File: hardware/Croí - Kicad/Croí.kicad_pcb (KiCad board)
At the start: 4 copper layers, 60 x 60 mm, 46 parts, among them J1 JTAG-10 PIN, J2 XT30PW-M, J3 ESQ-110-14-G-D, Q1 IPP060N06N, U1 W25Q128JVS, U2 ADXL375BCCZ, U3 STM32F072C8Tx, U4 BME680, U5 BMP390, U7 TLV70433DBVT, U8 TJA1051T-3, U9 LSM6DSO32TR

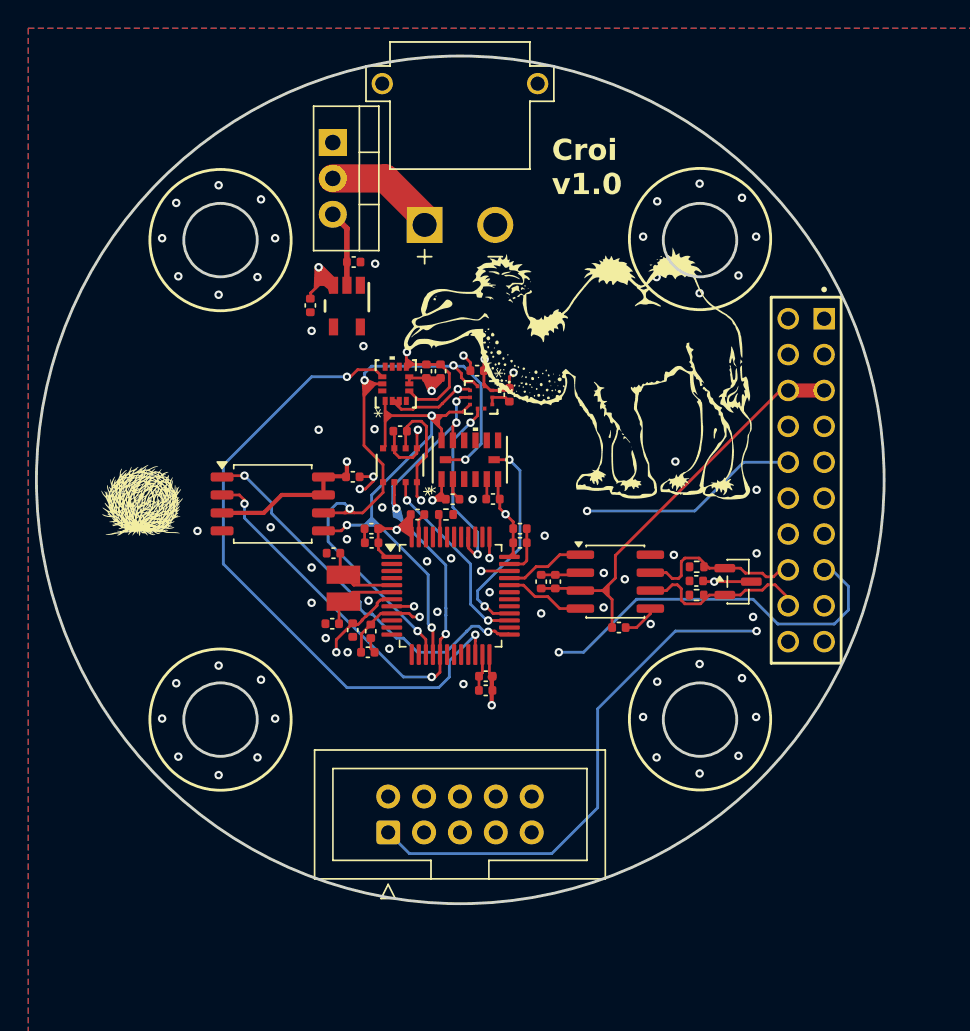
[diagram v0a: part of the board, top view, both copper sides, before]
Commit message: Started Applying Global Changes
1. Shape and screwholes
2. Mosfet
3. New Molex
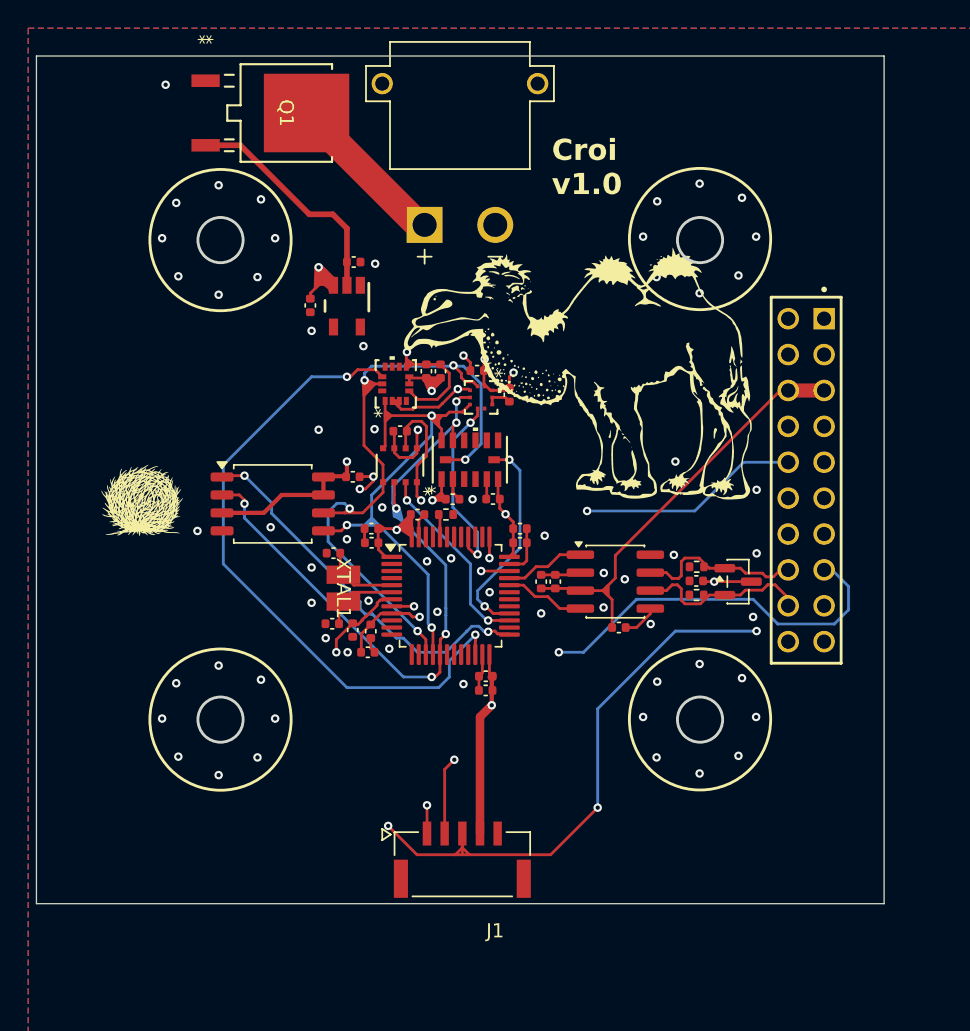
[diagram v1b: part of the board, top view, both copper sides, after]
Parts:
- J1: value JTAG-10 PIN -> 5023860570; footprint Connector_IDC:IDC-Header_2x05_P2.54mm_Vertical -> MOLEX:MOLEX_5023860570
- Q1: value IPP060N06N -> IPD90P04P4L04ATMA1; footprint Package_TO_SOT_THT:TO-220-3_Vertical -> footprints:PG-TO252-3-313_INF
- moved J1 5.63 mm to (73.0, 96.0), turned to 180 degrees
- moved Q1 3.90 mm to (60.5, 43.0)
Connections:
- J1 pad 1: NRST -> SWCLK2
- J1 pad 2: SWCLK2 -> SWDIO
- J1 pad 3: unconnected-(J1-Pin_3-Pad3) -> NRST
- J1 pad 4: SWDIO -> 3.3V
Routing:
- net VBAT: track 5.44 -> 16.5 mm
- net SWCLK2: track 48.4 -> 52.6 mm, vias 2 -> 3
- net NRST: track 62.8 -> 67.0 mm, vias 2 -> 4
- net Net-(Q1-D): track 7.66 -> 11.6 mm
- net SWDIO: track 55.3 -> 57.7 mm, vias 2 -> 3
- net 3.3V: track 154.3 -> 155.1 mm
- net (no net): vias 0 -> 1
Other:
- outline, holes or cut-outs redrawn

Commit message: Only missing one thing off the notion i believe, all 3d modlels should work
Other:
- board text added: "Croi v1.2"
- board text removed: "Croi v1.0"
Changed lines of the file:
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@@
 		(layer "Edge.Cuts")
 	)
-	(gr_text "Croi\nv1.0"
+	(gr_text "Croi\nv1.2"
 		(at 79.331 48.919 0)
 		(layer "F.SilkS")

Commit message: lots left to do, but good enough for render
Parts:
- removed U7: TLV70433DBVT, footprints:DBV0005A_M
- added 3v3: S2761-46R, footprints2:HARWIN_S2761-46R, F.Cu at (147.0, 79.8)
- added C+1: S2761-46R, footprints2:HARWIN_S2761-46R, F.Cu at (91.4, 73.6)
- added C-1: S2761-46R, footprints2:HARWIN_S2761-46R, F.Cu at (91.7, 78.8)
- added C14: 39pf, Capacitor_SMD:C_0402_1005Metric, F.Cu at (149.7, 63.5)
- added C16: 0.1uf, Capacitor_SMD:C_0402_1005Metric, F.Cu at (149.7, 65.5)
- added C29: 0.1uf, Capacitor_SMD:C_0402_1005Metric, F.Cu at (149.7, 71.4)
- added C30: 1uf, Capacitor_SMD:C_0402_1005Metric, F.Cu at (152.6, 63.5)
- added C31: 22uf, Capacitor_SMD:C_0402_1005Metric, F.Cu at (152.6, 65.5)
- added C32: 22uf, Capacitor_SMD:C_0402_1005Metric, F.Cu at (152.6, 67.5)
- added C33: 22uf, Capacitor_SMD:C_0402_1005Metric, F.Cu at (152.6, 69.4)
- added C34: 22uf, Capacitor_SMD:C_0402_1005Metric, F.Cu at (152.6, 71.4)
- added C35: 4.7uf, Capacitor_SMD:C_0402_1005Metric, F.Cu at (155.4, 63.5)
- added C36: 4.7uf, Capacitor_SMD:C_0402_1005Metric, F.Cu at (155.4, 65.5)
- added C37: 10uf, Capacitor_SMD:C_0402_1005Metric, F.Cu at (155.4, 67.5)
- added D1: BAT54C, Package_TO_SOT_SMD:SOT-23, F.Cu at (151.2, 80.7)
- added G***: LOGO, LOGO, F.Cu at (74.0, 88.5)
- added GND1: S2761-46R, footprints2:HARWIN_S2761-46R, F.Cu at (147.0, 82.3)
- added R10: 33.2kΩ, Resistor_SMD:R_0402_1005Metric, F.Cu at (146.8, 75.5)
- added R2: 10kΩ, Resistor_SMD:R_0402_1005Metric, F.Cu at (146.8, 63.5)
- added R3: 53.6kΩ, Resistor_SMD:R_0402_1005Metric, F.Cu at (146.8, 65.5)
- added R4: 0Ω, Resistor_SMD:R_0402_1005Metric, F.Cu at (146.8, 67.5)
- added R5: 0Ω, Resistor_SMD:R_0402_1005Metric, F.Cu at (146.8, 69.5)
- added R8: 499kΩ, Resistor_SMD:R_0402_1005Metric, F.Cu at (146.8, 71.5)
- added R9: 100kΩ, Resistor_SMD:R_0402_1005Metric, F.Cu at (146.8, 73.5)
- added U6: MPM3650CGQW-P, footprints2:QFN-24_MPM3650_MNP, F.Cu at (62.8, 63.3)
- added VR1: LT3045EDD_PBF, footprints2:SON50P300X300X80-11N, F.Cu at (63.9, 57.0)
- C21: value 100nF -> 22uf
- C23: value 1 uF -> 22uf
- moved C23 88.4 mm to (149.7, 69.4), turned to 0 degrees
- moved C21 85.5 mm to (149.7, 67.5)
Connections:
- C21 pad 1: VBAT -> GND
- C21 pad 2: GND -> /power/vin
- C23 pad 2: 3.3V -> /power/vin
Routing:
- net Net-(VR1-EN/UV): track 0.00 -> 19.3 mm
- net GND: track 46.4 -> 62.9 mm
- net 3.3V: track 155.1 -> 164.4 mm
- added copper zone on In3.Cu, net GND
- removed copper zone on In1.Cu, net GND
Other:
- copper layers 4 -> 6
- board text added: "SWCLK SWDIO NRST 3v3 GND"
- board text added: "croi-v1.0"
- board text removed: "Croi v1.2"

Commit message: running
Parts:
- removed the C35 at (155.4, 63.5)
- removed R10: 33.2kΩ, Resistor_SMD:R_0402_1005Metric
- removed the R4 at (146.8, 67.5)
- removed R5: 0Ω, Resistor_SMD:R_0402_1005Metric
- removed R8: 499kΩ, Resistor_SMD:R_0402_1005Metric
- removed VR1: LT3045EDD_PBF, footprints2:SON50P300X300X80-11N
- added 5VL: S2761-46R, footprints2:HARWIN_S2761-46R, F.Cu at (90.5, 97.2)
- added U7: TLV75533PDRV, Package_SON:WSON-6-1EP_2x2mm_P0.65mm_EP1x1.6mm, F.Cu at (90.2, 67.7)
- C35: renamed from C36; value 4.7uf -> 1uf
- C36: renamed from C37; value 10uf -> 1uf
- J2: value XT30PW-M -> 39-29-1048; footprint footprints:AMASS_XT30PW-M -> footprints2:MOLEX_39-29-1048
- moved D1 66.3 mm to (90.5, 53.8), turned to -90 degrees
- moved C35 65.7 mm to (89.7, 65.9), turned to 180 degrees
- moved C29 65.3 mm to (87.5, 66.4), turned to 180 degrees
- moved C33 65.2 mm to (87.5, 69.4), turned to 180 degrees
- moved C31 65.1 mm to (87.5, 67.4), turned to 180 degrees
- moved C32 65.1 mm to (87.5, 68.4), turned to 180 degrees
- moved GND 65.0 mm to (83.8, 97.2)
- moved C36 65.0 mm to (90.5, 69.6), turned to 180 degrees
- moved C23 62.9 mm to (88.5, 55.2)
- moved C34 62.6 mm to (87.4, 65.4), turned to 180 degrees
- moved 3V3 62.3 mm to (87.2, 97.2)
- moved C21 62.3 mm to (88.4, 56.2)
- moved C16 61.8 mm to (88.4, 57.2)
- moved C30 60.1 mm to (92.7, 58.2), turned to 90 degrees
- moved C14 58.0 mm to (91.7, 62.2), turned to 90 degrees
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- renumbered 3v3 to 3V3, C34 to C29, C33 to C31, C31 to C33, C29 to C34, C+1 to CAN+1, C-1 to CAN-1, GND1 to GND, R9 to R4
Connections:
- C14 pad 2: Net-(C14-Pad2) -> Net-(U6-FB)
- C30 pad 1: AGND -> GND
- J1 pad 1: SWCLK2 -> SWCLK
- J3 pad 01: unconnected-(J3-Pad01) -> GND
- J3 pad 02: unconnected-(J3-Pad02) -> GND
- J3 pad 03: GND -> unconnected-(J3-Pad03)
- J3 pad 04: GND -> unconnected-(J3-Pad03)
- J3 pad 05: 5VLOGIC -> unconnected-(J3-Pad03)
- J3 pad 06: 5VLOGIC -> unconnected-(J3-Pad03)
- J3 pad 07: GND -> unconnected-(J3-Pad03)
- J3 pad 08: GND -> unconnected-(J3-Pad03)
- J3 pad 09: unconnected-(J3-Pad09) -> GND
- J3 pad 10: SWCLK2 -> GND
- J3 pad 11: unconnected-(J3-Pad11) -> 5VLOGIC
- J3 pad 12: unconnected-(J3-Pad12) -> 5VLOGIC
- J3 pad 13: unconnected-(J3-Pad13) -> GND
- J3 pad 15: SWDIO -> GND
- J3 pad 17: NRST -> GND
- R2 pad 1: AGND -> GND
- R2 pad 2: Net-(C14-Pad2) -> Net-(U6-FB)
- R3 pad 1: Net-(C14-Pad2) -> Net-(U6-FB)
- U6 pad 16: Net-(U6-EN) -> /power/vin
- U6 pad 18: AGND -> GND
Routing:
- net SWDIO: track 57.7 -> 0.00 mm, vias 3 -> 0
- net NRST: track 67.0 -> 22.4 mm, vias 4 -> 1
- net 3.3V: track 164.4 -> 144.3 mm, vias 12 -> 13
- net /power/vin: track 0.00 -> 19.8 mm, vias 0 -> 4
- net unconnected-(J3-Pad03): track 0.00 -> 17.8 mm
- net SWCLK2: track 52.6 -> 34.9 mm, vias 3 -> 1
- net VBAT: track 16.5 -> 0.00 mm
- net Net-(U6-VCC): track 0.00 -> 10.8 mm, vias 0 -> 2
- net GND: track 62.9 -> 71.8 mm, vias 71 -> 158
- net Net-(U7-EN): track 19.3 -> 12.1 mm
- net 5VLOGIC: track 30.0 -> 26.1 mm, vias 0 -> 1
- net Net-(U6-FB): track 0.00 -> 3.86 mm
- net Net-(Q1-D): track 11.6 -> 12.3 mm
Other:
- outline, holes or cut-outs redrawn

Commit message: clean asf
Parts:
- added G***: LOGO, LOGO, F.Cu at (44.8, 93.0)
- moved G*** 68.1 mm to (96.7, 90.5)
- moved G*** 34.9 mm to (59.2, 96.0)
- renumbered CAN+1 to CAN+, CAN-1 to CAN-
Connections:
- D1 pad 1: VBAT_Local -> VBAT
- D1 pad 2: 5V_LOGIC -> 5VLOGIC
- U3 pad 37: SWCLK2 -> SWCLK
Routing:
- net 5VLOGIC: track 26.1 -> 74.8 mm, vias 1 -> 3
- net 3.3V: track 144.3 -> 180.9 mm
- net SWCLK2: track 34.9 -> 0.00 mm, vias 1 -> 0
- net SWCLK: track 0.00 -> 21.4 mm, vias 0 -> 2
- net SWDIO: track 0.00 -> 20.4 mm, vias 0 -> 2
- net VBAT: track 0.00 -> 6.86 mm
- net /power/vin: track 19.8 -> 13.8 mm
- net Net-(Q1-D): track 12.3 -> 11.1 mm
- net GND: vias 158 -> 157
- net (no net): vias 1 -> 0
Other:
- board text added: "If you are reading this, Then you are reading this."
